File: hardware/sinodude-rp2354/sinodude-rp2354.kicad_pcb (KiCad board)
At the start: 2 copper layers, 75 x 40 mm, 93 parts, among them J1 USB-C, J2 SWD TC2030-IDC latching, J4 DUT, Q1 2N7002, SW1 BOOTSEL, SW2 RESET, U1 RP2354A, U2 AMS1117-3.3, U3 TPS2114APW, U4 SN74LVC8T245PW, U5 SN74LVC1T45DBV, U6 SN74LVC1T45DBV, Y1 12MHz/CL10pF/ESR50R/ABM8-272-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

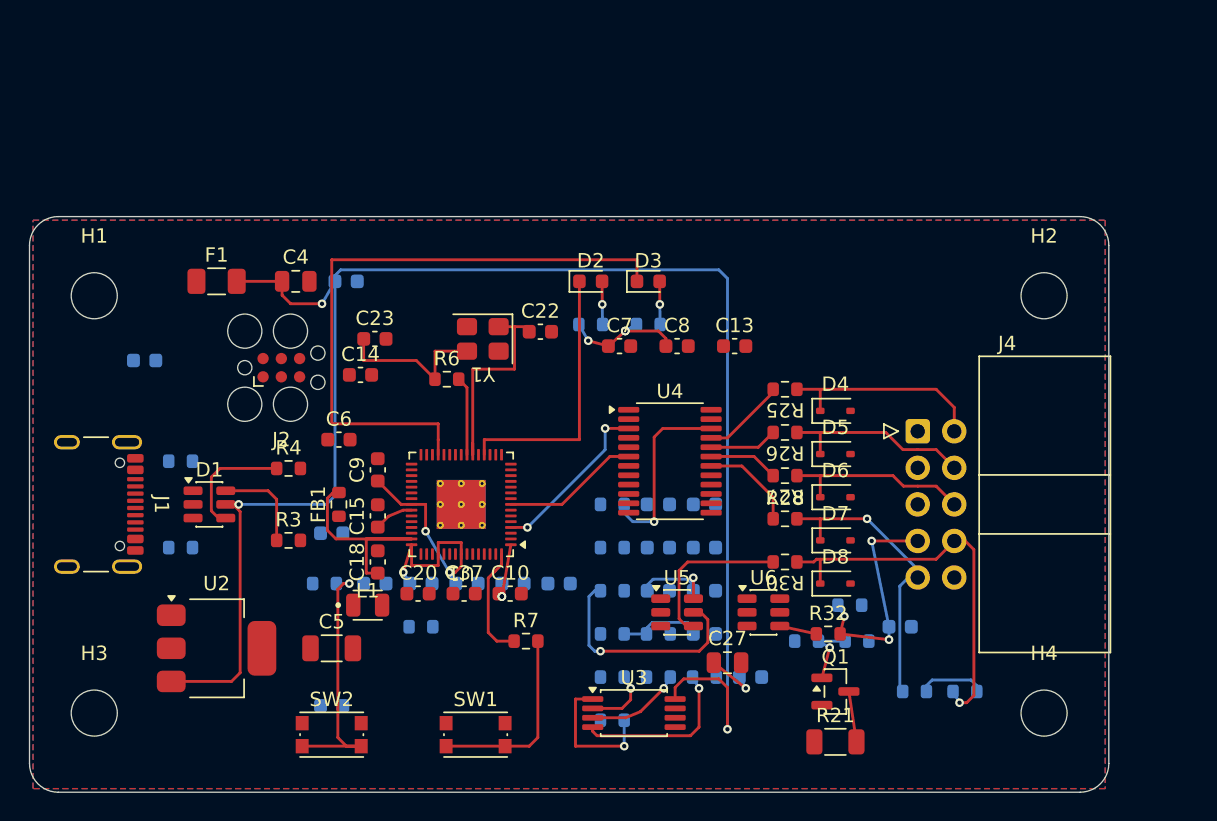
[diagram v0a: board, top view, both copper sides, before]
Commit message: hardware: route the RP2354 board on a 68x36 mm two-layer outline
Shrinks the outline from 75x40 mm and re-floorplans into blocks: USB and the
3V3 regulator west, SWD and clock north, target supply and level shifters east,
discharge south-east, both buttons together under U4. M3 mounting holes.

Reassigns U1's GPIOs so the JTAG group and DATA/KEY leave the east column in the
order U4, U5/U6 and the DUT header need them. Assigned the other way round they
have to cross inside the 0.4 mm pad ring, where there is no room.

Design rules drop to 0.15 mm track and clearance with board minimums set to
JLCPCB's two-layer capability, which is what makes the QFN escapes fit. Ground
pours use solid pad connections, since thermal spokes starve on two layers, and
are stitched together.

The Tag-Connect, the USB pair and the VBUS bridge are routed by hand: J2's leg
holes leave one single-track channel per pad and which channel a pad may use is
forced by geometry, so no autorouter finds them.

DRC is clean. Two connections remain open, KEY_DIR and U1's ground pin 47, both
noted in the README.
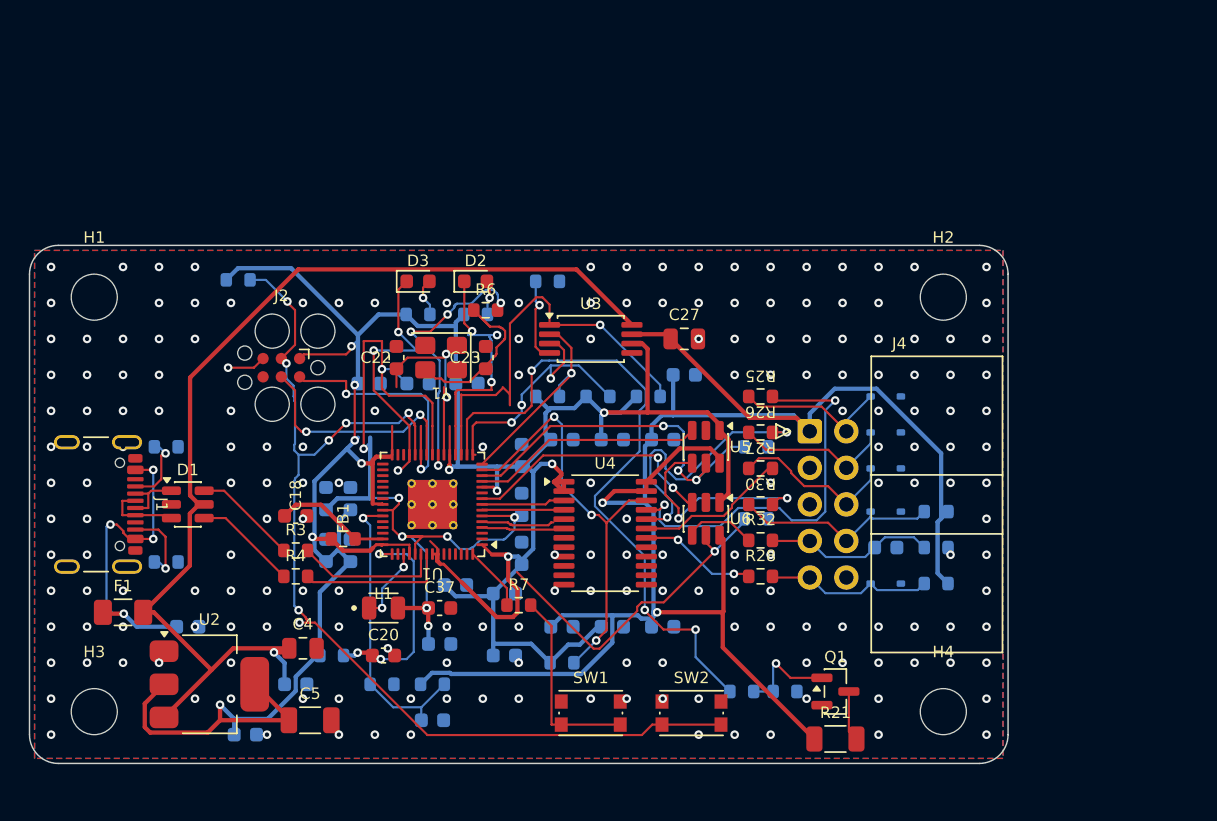
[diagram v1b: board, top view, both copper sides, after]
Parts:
- C10, C13, C14, C15, C6, C7, C8, C9, D4, D5, D6, D7, D8: moved to B.Cu
- moved R15 29.6 mm to (136.0, 104.5)
- moved C25 28.2 mm to (118.5, 132.5)
- moved U3 26.2 mm to (139.0, 108.5)
- moved C4 25.5 mm to (119.0, 130.0)
- moved SW2 25.0 mm to (146.0, 134.5)
- moved F1 23.9 mm to (106.5, 127.5)
- moved C27 22.7 mm to (145.5, 108.5)
- moved R16 22.6 mm to (143.0, 112.5)
- moved R8 21.9 mm to (114.5, 104.4)
- moved C28 21.5 mm to (145.5, 111.0)
- moved R13 20.0 mm to (136.0, 112.5)
- moved R14 19.9 mm to (139.5, 112.5)
- moved C29 19.8 mm to (128.0, 135.0)
- moved R18 19.5 mm to (124.5, 132.5)
- moved C1 18.7 mm to (111.0, 128.5)
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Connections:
- U1 pad 10: DATA_DIR -> KEY_DIR
- U1 pad 12: KEY_3V3 -> DATA_3V3
- U1 pad 13: KEY_DIR -> DATA_DIR
- U1 pad 4: TCK_3V3 -> NRST_3V3
- U1 pad 5: TDI_3V3 -> TMS_3V3
- U1 pad 7: TMS_3V3 -> TDI_3V3
- U1 pad 8: NRST_3V3 -> TCK_3V3
- U1 pad 9: DATA_3V3 -> KEY_3V3
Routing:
- net +3V3: track 38.4 -> 209.6 mm, vias 8 -> 11
- net VTGT: track 15.1 -> 126.6 mm
- net +1V1: track 2.75 -> 63.7 mm, vias 0 -> 8
- net RUN: track 18.1 -> 71.5 mm, vias 1 -> 7
- net VTGT_DISCH: track 0.00 -> 46.5 mm, vias 0 -> 3
- net +5V: track 116.4 -> 74.7 mm, vias 3 -> 1
- net LED_ERR: track 43.7 -> 18.4 mm, vias 0 -> 3
- net KEY_DIR: track 0.00 -> 23.4 mm, vias 0 -> 1
- net VBUS: track 0.00 -> 22.3 mm, vias 0 -> 4
- net TCK_B: track 5.92 -> 27.9 mm, vias 0 -> 2
- net SWDIO: track 0.00 -> 20.2 mm, vias 0 -> 2
- net VTGT_STAT: track 9.66 -> 29.8 mm
- net KEY_3V3: track 0.00 -> 17.8 mm, vias 0 -> 2
- net XLAT_OE: track 13.0 -> 29.8 mm, vias 1 -> 3
- net SWCLK: track 0.00 -> 16.1 mm, vias 0 -> 2
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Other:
- board size 75 x 40 mm -> 68 x 36 mm

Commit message: hardware: finish routing the RP2354 board
Every net is now routed: DRC reports 0 errors and no real open connections
(the 12 remaining unconnected items are GND pour islands, and the zones drop
isolated islands). 919 track segments, 268 vias.

The last few links needed placement changes rather than more routing:

- L1 moves 1.4 mm south, widening the band below U1 from 2.3 to 3.7 mm so the
  south-row escapes and the USB lane stop competing for it. GND pin 47's via
  window had been 0.025 mm wide.
- The target discharge switch (Q1, R21) moves under U6, next to the VTGT
  network it switches, instead of sitting alone at the board edge.
- KEY_3V3 crosses under U4 on the free back-layer lane at y = 118.06.

USB_DM/USB_DP are routed as a coupled pair, 0.15 mm on a 0.25 mm gap, with no
via between J1 and U1, under a new USB netclass.

No via lands on a Tag-Connect pad. A same-net via there passes DRC but leaves
a dimple under the pogo pin, so both routers now treat every surface pad as a
via keepout.
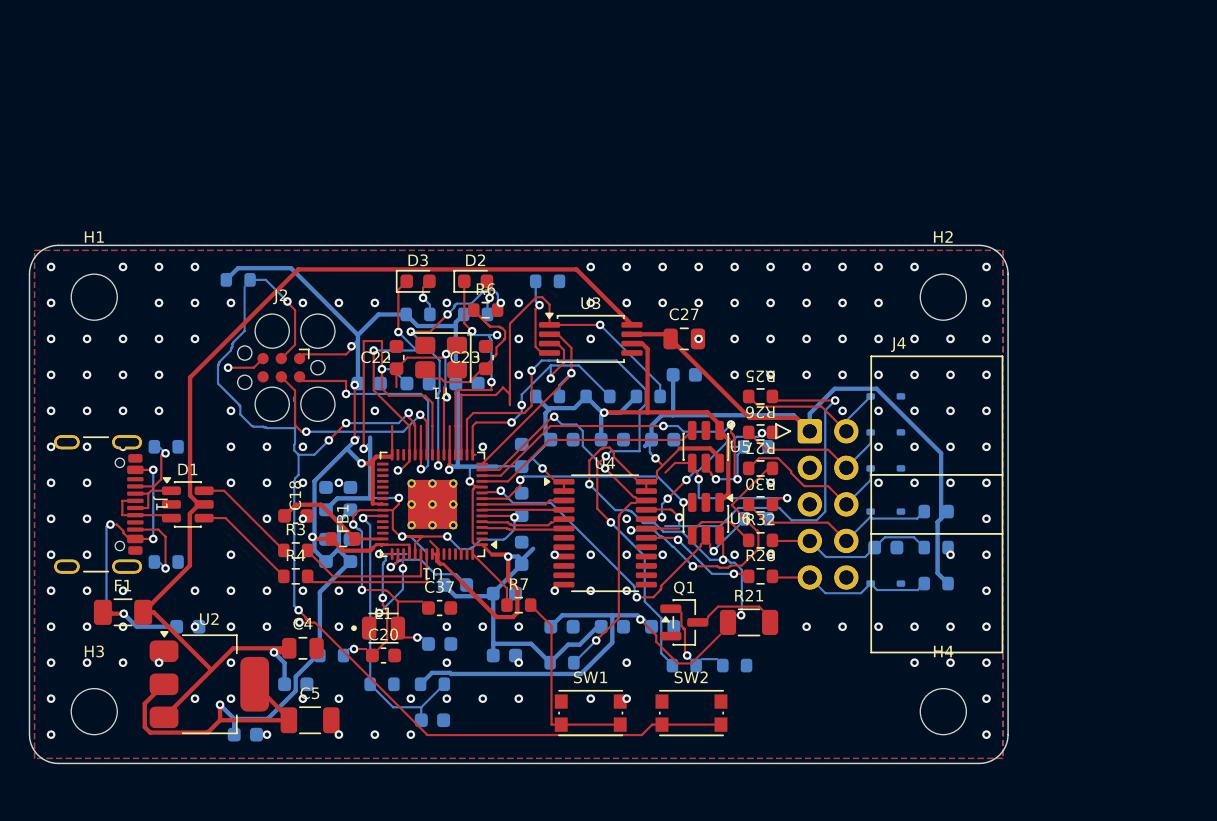
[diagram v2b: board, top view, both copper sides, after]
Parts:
- moved Q1 11.5 mm to (145.5, 128.2)
- moved R21 10.1 mm to (150.0, 128.2)
- moved R19 4.39 mm to (145.5, 131.2)
- moved R20 3.94 mm to (149.0, 131.2)
- moved L1 1.40 mm to (124.6, 128.6)
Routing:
- net RUN: track 71.5 -> 83.4 mm, vias 7 -> 6
- net TMS_B: track 10.6 -> 20.8 mm, vias 0 -> 2
- net TDI_B: track 20.0 -> 10.6 mm, vias 2 -> 4
- net VTGT: track 126.6 -> 119.0 mm, vias 2 -> 5
- net GND: track 2.69 -> 9.08 mm, vias 191 -> 172
- net +3V3: track 209.6 -> 204.0 mm
- net +1V1: track 63.7 -> 68.5 mm, vias 8 -> 9
- net VREG_AVDD: track 15.4 -> 11.1 mm
- net VTGT_DISCH: track 46.5 -> 42.2 mm
- net DATA_B: track 15.1 -> 11.4 mm
- net DATA_DIR: track 25.7 -> 28.1 mm, vias 3 -> 4
- net Net-(Q1-G): track 6.98 -> 4.68 mm
- net KEY_3V3: track 17.8 -> 16.2 mm
- net XLAT_OE: track 29.8 -> 28.3 mm
- net TCK_B: track 27.9 -> 27.1 mm
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
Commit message: hardware: clear every DRC and ERC warning on the RP2354 board
The board reported 0 errors but 247 warnings and 12 "unconnected" items.
Both reports are now empty at every severity.

The unconnected items were not cosmetic. They were ratsnest lines between
ground pour regions, and ten GND pads sat in pockets of pour that reached
nothing else, so those pads were floating: U5 and U6's ground pins, the
crystal's, the ESD diode's, and six decoupling caps'. On two layers a dense
signal field cuts the pour into islands, and a pad stranded in one still reads
as routed unless you look at what the zone-to-zone line actually means.

Reconnecting them needed more than stitching vias:

- DATA_DIR is rerouted, which frees C32 and U5's ground pin.
- One 4.2 mm length of +3V3 east of U4 drops to 0.20 mm, opening the slot U5's
  ground escapes through. It carries the shifters' A-side supply, a few mA.
- The +3V3 climb between C6 and C12 moves, and the two caps' ground pads are
  tied directly, which is what finally reaches C12.

Also in the copper: dead track stubs and vias removed (a few were load-bearing
and were trimmed back to their junction instead), RUN's escape from its via
rebuilt as one 45 degree run, and seven segments snapped to exact 45 degrees.

The 89 library mismatches were real drift, not noise: the board's footprints
carried no `attr`, no 3D model, and float-rounded coordinates from an earlier
flip. All three are restored from the libraries, so the check is meaningful
again. Three footprints genuinely differ from stock and are now project copies
in footprints/sinodude.pretty: the USB-C receptacle (corner ground pads trimmed
to clear the shell holes), the DUT header (pin 1 arrow off R26's pad), and the
QFN (thermal vias at JLCPCB's minimum drill). J2 regains the stock keepout
zone, so "no via on a Tag-Connect pad" is enforced by the footprint.

The 53 silkscreen warnings are fixed by placing reference designators: they are
clear of pads and of each other, and all rea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
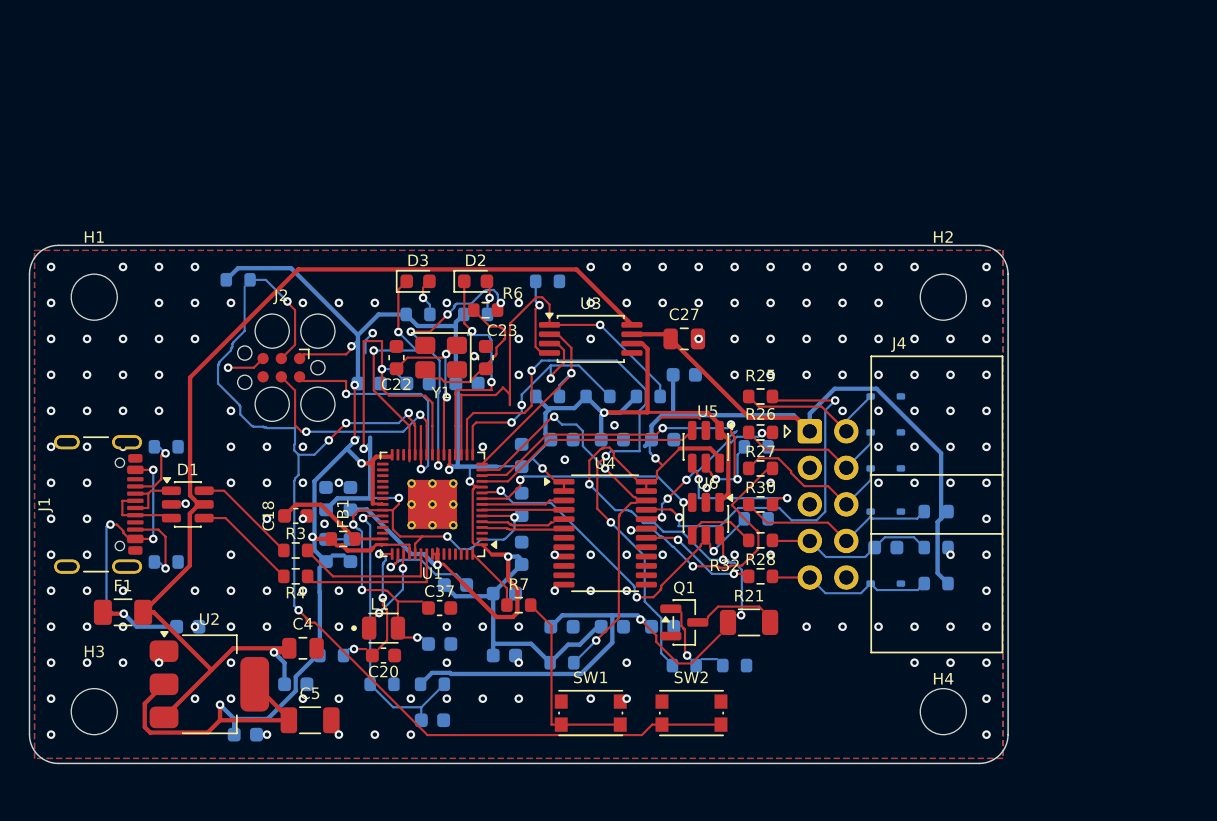
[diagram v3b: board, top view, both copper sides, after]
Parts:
- J1: footprint Connector_USB:USB_C_Receptacle_GCT_USB4105-xx-A_16P_TopMnt_Horizontal -> sinodude:USB_C_Receptacle_GCT_USB4105-xx-A_16P_TopMnt_Horizontal
- J4: footprint Connector_IDC:IDC-Header_2x05_P2.54mm_Horizontal -> sinodude:IDC-Header_2x05_P2.54mm_Horizontal
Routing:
- net GND: track 9.08 -> 16.4 mm, vias 172 -> 177
- net +3V3: track 204.0 -> 199.0 mm, vias 11 -> 12
- net +1V1: track 68.5 -> 64.9 mm, vias 9 -> 8
- net RUN: track 83.4 -> 80.8 mm, vias 6 -> 5
- net TMS_B: track 20.8 -> 18.5 mm
- net DATA_B: track 11.4 -> 9.23 mm
- net DATA_DIR: track 28.1 -> 26.3 mm
- net XIN: track 14.2 -> 12.4 mm
- net VREG_AVDD: track 11.1 -> 9.69 mm
- net LED_ERR: track 18.4 -> 17.3 mm, vias 3 -> 2
- net Net-(C23-Pad1): track 11.8 -> 10.8 mm
- net TCK_B: track 27.1 -> 26.2 mm
- net LED_ACT: track 16.9 -> 16.4 mm, vias 3 -> 2

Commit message: hardware: pull the outlying parts in, fill the stitching grid, label the switches
C26 sat 2 mm off the south edge with nothing around it; it is the 3V3 output
cap and now sits under U2 where it belongs. R8, R15 and C29 were out at the
edge the same way: R8 moves onto the +3V3 run it pulls RUN up to (its pad now
lands on that track directly), R15 beside U3's ILIM pin, C29 next to the VTGT
sense divider. RUN's escape from the Tag-Connect is unchanged; the branch that
used to detour through R8's old position is rebuilt to reach the trunk.

The ground stitching lattice stopped short of the south-east corner, leaving
roughly 25 x 7 mm of pour tied in only at its edges. Every free point of the
2.5 mm lattice now carries a via where both pours are clear: 198 ground vias,
up from 177, and the gap under J4 and the buttons is filled.

SW1 and SW2 show BOOTSEL and RESET on the silkscreen. It is their Value field
rather than free-standing text, so the legend cannot drift from the schematic.

H1 and H2's labels were off the board edge entirely and H3's was floating 4 mm
from its hole. All four now sit on the inboard side of their hole.

DRC and ERC stay clean at every severity, the ground net is still one piece of
copper, and every track is still on 0, 45 or 90 degrees.
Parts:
- moved R8 5.12 mm to (119.5, 105.5), turned to 180 degrees
- moved C29 4.85 mm to (125.4, 130.9)
- moved R15 3.14 mm to (136.5, 107.6)
- moved C26 3.04 mm to (114.5, 133.0)
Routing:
- net +3V3: track 199.0 -> 181.2 mm, vias 12 -> 13
- net Net-(U3-ILIM): track 5.92 -> 1.64 mm
- net RUN: track 80.8 -> 83.6 mm
- net VTGT_SENSE: track 20.6 -> 19.6 mm
- net GND: vias 177 -> 198
